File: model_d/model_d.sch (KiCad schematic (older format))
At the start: 50 parts, among them J1 Conn_01x16_Male, J2 Conn_01x08_Male, SW1 SW_Cap, SW10 SW_Cap, SW11 SW_Cap, SW12 SW_Cap, SW13 SW_Cap, SW14 SW_Cap, SW15 SW_Cap, SW16 SW_Cap, SW17 SW_Cap, SW18 SW_Cap, SW19 SW_Cap, SW2 SW_Cap, SW20 SW_Cap, SW21 SW_Cap, SW22 SW_Cap, SW23 SW_Cap, SW24 SW_Cap, SW25 SW_Cap, SW26 SW_Cap, SW27 SW_Cap, SW28 SW_Cap, SW29 SW_Cap, SW3 SW_Cap, SW30 SW_Cap, SW31 SW_Cap, SW32 SW_Cap, SW33 SW_Cap, SW34 SW_Cap, SW35 SW_Cap, SW36 SW_Cap, SW37 SW_Cap, SW38 SW_Cap, SW39 SW_Cap, SW4 SW_Cap, SW40 SW_Cap, SW41 SW_Cap, SW42 SW_Cap, SW43 SW_Cap, SW44 SW_Cap, SW45 SW_Cap, SW46 SW_Cap, SW47 SW_Cap, SW48 SW_Cap, SW5 SW_Cap, SW6 SW_Cap, SW7 SW_Cap, SW8 SW_Cap, SW9 SW_Cap

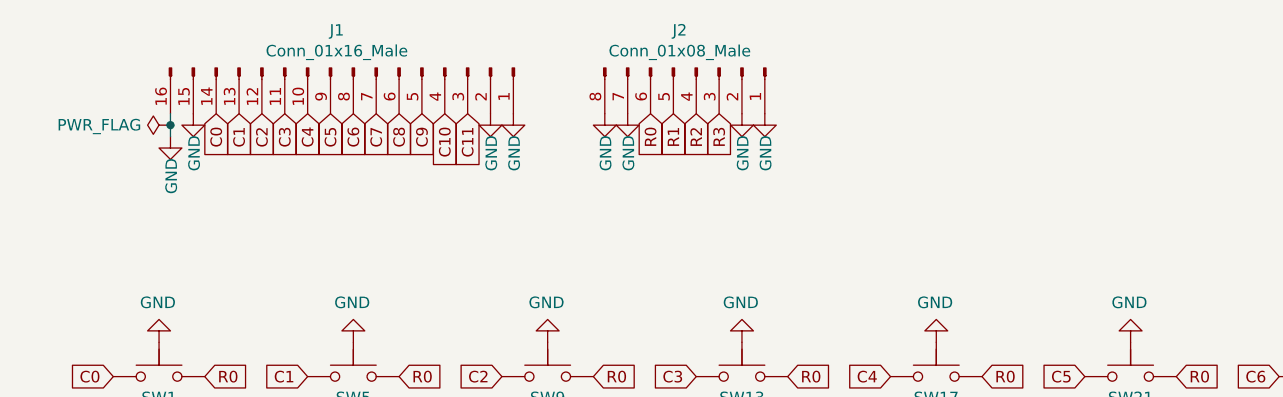
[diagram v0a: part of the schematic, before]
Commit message: complete place & route, add gnd plate
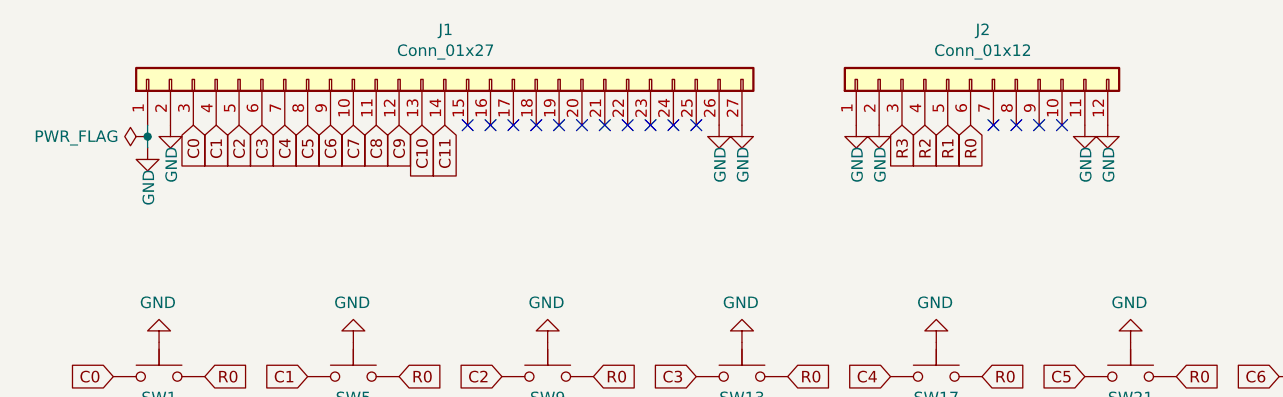
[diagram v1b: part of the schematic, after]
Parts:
- removed J1: Conn_01x16_Male, Connector_PinHeader_2.54mm:PinHeader_1x16_P2.54mm_Vertical, symbol Connector:Conn_01x16_Male
- removed J2: Conn_01x08_Male, Connector_PinHeader_2.54mm:PinHeader_1x08_P2.54mm_Vertical, symbol Connector:Conn_01x08_Male
- added J1: Conn_01x27, Connector_PinHeader_2.54mm:PinHeader_1x27_P2.54mm_Vertical, symbol Connector_Generic:Conn_01x27
- added J2: Conn_01x12, Connector_PinHeader_2.54mm:PinHeader_1x12_P2.54mm_Vertical, symbol Connector_Generic:Conn_01x12
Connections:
- net C0: now also J1.3 (Pin_3)
- net C1: now also J1.4 (Pin_4)
- net C10: now also J1.13 (Pin_13)
- net C11: now also J1.14 (Pin_14)
- net C2: now also J1.5 (Pin_5)
- net C3: now also J1.6 (Pin_6)
- net C4: now also J1.7 (Pin_7)
- net C5: now also J1.8 (Pin_8)
- net C6: now also J1.9 (Pin_9)
- net C7: now also J1.10 (Pin_10)
- net C8: now also J1.11 (Pin_11)
- net C9: now also J1.12 (Pin_12)
- net GND: now also J1.1 (Pin_1), J1.2 (Pin_2), J1.26 (Pin_26), J1.27 (Pin_27), J2.1 (Pin_1), J2.11 (Pin_11), J2.12 (Pin_12), J2.2 (Pin_2)
- net R0: now also J2.6 (Pin_6)
- net R1: now also J2.5 (Pin_5)
- net R2: now also J2.4 (Pin_4)
- net R3: now also J2.3 (Pin_3)
- no-connect marks 0 -> 15
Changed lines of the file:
@@
-$EndComp
-$Comp
-L Connector:Conn_01x16_Male J1
-U 1 1 6176F4F2
-P 2000 1000
-F 0 "J1" V 1835 928 50  0000 C CNN
-F 1 "Conn_01x16_Male" V 1926 928 50  0000 C CNN
-F 2 "Connector_PinHeader_2.54mm:PinHeader_1x16_P2.54mm_Vertical" H 2000 1000 50  0001 C CNN
-F 3 "~" H 2000 1000 50  0001 C CNN
-	1    2000 1000
-	0    1    1    0
 $EndComp
 $Comp
 L power:GND #PWR05
 U 1 1 61773EA7
-P 1200 1300
-F 0 "#PWR05" H 1200 1050 50  0001 C CNN
-F 1 "GND" V 1205 1127 50  0000 C CNN
-F 2 "" H 1200 1300 50  0001 C CNN
-F 3 "" H 1200 1300 50  0001 C CNN
-	1    1200 1300
+P 1100 1350
+F 0 "#PWR05" H 1100 1100 50  0001 C CNN
+F 1 "GND" V 1105 1177 50  0000 C CNN
+F 2 "" H 1100 1350 50  0001 C CNN
+F 3 "" H 1100 1350 50  0001 C CNN
+	1    1100 1350
 	1    0    0    -1
 $EndComp
@@
 L power:GND #PWR06
 U 1 1 61775637
-P 1300 1200
-F 0 "#PWR06" H 1300 950 50  0001 C CNN
-F 1 "GND" V 1305 1027 50  0000 C CNN
-F 2 "" H 1300 1200 50  0001 C CNN
-F 3 "" H 1300 1200 50  0001 C CNN
-	1    1300 1200
+P 1200 1250
+F 0 "#PWR06" H 1200 1000 50  0001 C CNN
+F 1 "GND" V 1205 1077 50  0000 C CNN
+F 2 "" H 1200 1250 50  0001 C CNN
+F 3 "" H 1200 1250 50  0001 C CNN
+	1    1200 1250
 	1    0    0    -1
 $EndComp
@@
 L power:GND #PWR011
 U 1 1 61775AD8
-P 2600 1200
-F 0 "#PWR011" H 2600 950 50  0001 C CNN
-F 1 "GND" V 2605 1027 50  0000 C CNN
-F 2 "" H 2600 1200 50  0001 C CNN
-F 3 "" H 2600 1200 50  0001 C CNN
-	1    2600 1200
+P 3600 1250
+F 0 "#PWR011" H 3600 1000 50  0001 C CNN
+F 1 "GND" V 3605 1077 50  0000 C CNN
+F 2 "" H 3600 1250 50  0001 C CNN
+F 3 "" H 3600 1250 50  0001 C CNN
+	1    3600 1250
 	1    0    0    -1
 $EndComp
@@
 L power:GND #PWR012
 U 1 1 61775FCF
-P 2700 1200
-F 0 "#PWR012" H 2700 950 50  0001 C CNN
-F 1 "GND" V 2705 1027 50  0000 C CNN
-F 2 "" H 2700 1200 50  0001 C CNN
-F 3 "" H 2700 1200 50  0001 C CNN
-	1    2700 1200
+P 3700 1250
+F 0 "#PWR012" H 3700 1000 50  0001 C CNN
+F 1 "GND" V 3705 1077 50  0000 C CNN
+F 2 "" H 3700 1250 50  0001 C CNN
+F 3 "" H 3700 1250 50  0001 C CNN
+	1    3700 1250
 	1    0    0    -1
 $EndComp
-Text GLabel 1400 1200 3    50   Input ~ 0
+Text GLabel 1300 1250 3    50   Input ~ 0
 C0
-Text GLabel 1500 1200 3    50   Input ~ 0
+Text GLabel 1400 1250 3    50   Input ~ 0
 C1
-Text GLabel 1600 1200 3    50   Input ~ 0
+Text GLabel 1500 1250 3    50   Input ~ 0
 C2
-Text GLabel 1800 1200 3    50   Input ~ 0
+Text GLabel 1700 1250 3    50   Input ~ 0
 C4
-Text GLabel 1900 1200 3    50   Input ~ 0
+Text GLabel 1800 1250 3    50   Input ~ 0
 C5
-Text GLabel 2000 1200 3    50   Input ~ 0
+Text GLabel 1900 1250 3    50   Input ~ 0
 C6
-Text GLabel 2100 1200 3    50   Input ~ 0
+Text GLabel 2000 1250 3    50   Input ~ 0
 C7
-Text GLabel 2200 1200 3    50   Input ~ 0
+Text GLabel 2100 1250 3    50   Input ~ 0
 C8
-Text GLabel 2300 1200 3    50   Input ~ 0
+Text GLabel 2200 1250 3    50   Input ~ 0
 C9
-Text GLabel 2400 1200 3    50   Input ~ 0
+Text GLabel 2300 1250 3    50   Input ~ 0
 C10
-Text GLabel 2500 1200 3    50   Input ~ 0
+Text GLabel 2400 1250 3    50   Input ~ 0
 C11
-Text GLabel 1700 1200 3    50   Input ~ 0
+Text GLabel 1600 1250 3    50   Input ~ 0
 C3
-$Comp
-L Connector:Conn_01x08_Male J2
-U 1 1 61788BE2
-P 3500 1000
-F 0 "J2" V 3335 928 50  0000 C CNN
-F 1 "Conn_01x08_Male" V 3426 928 50  0000 C CNN
-F 2 "Connector_PinHeader_2.54mm:PinHeader_1x08_P2.54mm_Vertical" H 3500 1000 50  0001 C CNN
-F 3 "~" H 3500 1000 50  0001 C CNN
-	1    3500 1000
-	0    1    1    0
-$EndComp
 $Comp
 L power:GND #PWR017
 U 1 1 6178BA2D
-P 3100 1200
-F 0 "#PWR017" H 3100 950 50  0001 C CNN
-F 1 "GND" V 3105 1027 50  0000 C CNN
-F 2 "" H 3100 1200 50  0001 C CNN
-F 3 "" H 3100 1200 50  0001 C CNN
-	1    3100 1200
+P 4200 1250
+F 0 "#PWR017" H 4200 1000 50  0001 C CNN
+F 1 "GND" V 4205 1077 50  0000 C CNN
+F 2 "" H 4200 1250 50  0001 C CNN
+F 3 "" H 4200 1250 50  0001 C CNN
+	1    4200 1250
 	1    0    0    -1
 $EndComp
@@
 L power:GND #PWR018
 U 1 1 6178C020
-P 3200 1200
-F 0 "#PWR018" H 3200 950 50  0001 C CNN
-F 1 "GND" V 3205 1027 50  0000 C CNN
-F 2 "" H 3200 1200 50  0001 C CNN
-F 3 "" H 3200 1200 50  0001 C CNN
-	1    3200 1200
+P 4300 1250
+F 0 "#PWR018" H 4300 1000 50  0001 C CNN
+F 1 "GND" V 4305 1077 50  0000 C CNN
+F 2 "" H 4300 1250 50  0001 C CNN
+F 3 "" H 4300 1250 50  0001 C CNN
+	1    4300 1250
 	1    0    0    -1
 $EndComp
@@
 L power:GND #PWR019
 U 1 1 6178C499
-P 3700 1200
-F 0 "#PWR019" H 3700 950 50  0001 C CNN
-F 1 "GND" V 3705 1027 50  0000 C CNN
-F 2 "" H 3700 1200 50  0001 C CNN
-F 3 "" H 3700 1200 50  0001 C CNN
-	1    3700 1200
+P 5200 1250
+F 0 "#PWR019" H 5200 1000 50  0001 C CNN
+F 1 "GND" V 5205 1077 50  0000 C CNN
+F 2 "" H 5200 1250 50  0001 C CNN
+F 3 "" H 5200 1250 50  0001 C CNN
+	1    5200 1250
 	1    0    0    -1
 $EndComp
@@
 L power:GND #PWR024
 U 1 1 6178CA31
-P 3800 1200
-F 0 "#PWR024" H 3800 950 50  0001 C CNN
-F 1 "GND" V 3805 1027 50  0000 C CNN
-F 2 "" H 3800 1200 50  0001 C CNN
-F 3 "" H 3800 1200 50  0001 C CNN
-	1    3800 1200
+P 5300 1250
+F 0 "#PWR024" H 5300 1000 50  0001 C CNN
+F 1 "GND" V 5305 1077 50  0000 C CNN
+F 2 "" H 5300 1250 50  0001 C CNN
+F 3 "" H 5300 1250 50  0001 C CNN
+	1    5300 1250
 	1    0    0    -1
 $EndComp
-Text GLabel 3300 1200 3    50   Input ~ 0
+Text GLabel 4700 1250 3    50   Input ~ 0
 R0
-Text GLabel 3400 1200 3    50   Input ~ 0
+Text GLabel 4600 1250 3    50   Input ~ 0
 R1
-Text GLabel 3500 1200 3    50   Input ~ 0
+Text GLabel 4500 1250 3    50   Input ~ 0
 R2
-Text GLabel 3600 1200 3    50   Input ~ 0
+Text GLabel 4400 1250 3    50   Input ~ 0
 R3
 $Comp
 L power:PWR_FLAG #FLG0101
 U 1 1 617950E2
-P 1200 1250
-F 0 "#FLG0101" H 1200 1325 50  0001 C CNN
-F 1 "PWR_FLAG" V 1200 1377 50  0000 L CNN
-F 2 "" H 1200 1250 50  0001 C CNN
-F 3 "~" H 1200 1250 50  0001 C CNN
-	1    1200 1250
+P 1100 1300
+F 0 "#FLG0101" H 1100 1375 50  0001 C CNN
+F 1 "PWR_FLAG" V 1100 1427 50  0000 L CNN
+F 2 "" H 1100 1300 50  0001 C CNN
+F 3 "~" H 1100 1300 50  0001 C CNN
+	1    1100 1300
 	0    -1   -1   0
 $EndComp
 Wire Wire Line
-	1200 1300 1200 1250
+	1100 1350 1100 1300
 Wire Wire Line
-	1200 1250 1200 1200
-Connection ~ 1200 1250
+	1100 1300 1100 1250
+$Comp
+L Connector_Generic:Conn_01x27 J1
+U 1 1 616B3F4A
+P 2400 1050
+F 0 "J1" V 2617 1046 50  0000 C CNN
+F 1 "Conn_01x27" V 2526 1046 50  0000 C CNN
+F 2 "Connector_PinHeader_2.54mm:PinHeader_1x27_P2.54mm_Vertical" H 2400 1050 50  0001 C CNN
+F 3 "~" H 2400 1050 50  0001 C CNN
+	1    2400 1050
+	0    -1   -1   0
+$EndComp
+Connection ~ 1100 1300
+NoConn ~ 2500 1250
+NoConn ~ 2600 1250
+NoConn ~ 2700 1250
+NoConn ~ 2800 1250
+NoConn ~ 2900 1250
+NoConn ~ 3000 1250
+NoConn ~ 3100 1250
+NoConn ~ 3200 1250
+NoConn ~ 3300 1250
+NoConn ~ 3400 1250
+NoConn ~ 3500 1250
+$Comp
+L Connector_Generic:Conn_01x12 J2
+U 1 1 61709475
+P 4700 1050
+F 0 "J2" V 4917 996 50  0000 C CNN
+F 1 "Conn_01x12" V 4826 996 50  0000 C CNN
+F 2 "Connector_PinHeader_2.54mm:PinHeader_1x12_P2.54mm_Vertical" H 4700 1050 50  0001 C CNN
+F 3 "~" H 4700 1050 50  0001 C CNN
+	1    4700 1050
+	0    -1   -1   0
+$EndComp
+NoConn ~ 4800 1250
+NoConn ~ 4900 1250
+NoConn ~ 5000 1250
+NoConn ~ 5100 1250
 $EndSCHEMATC

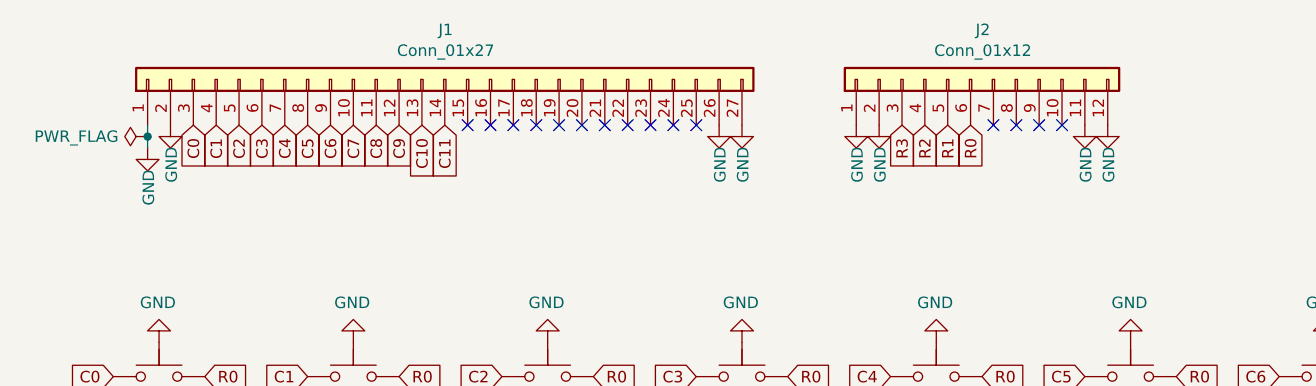
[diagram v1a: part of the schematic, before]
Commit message: add m3 mounting holes, increase size to 113x244
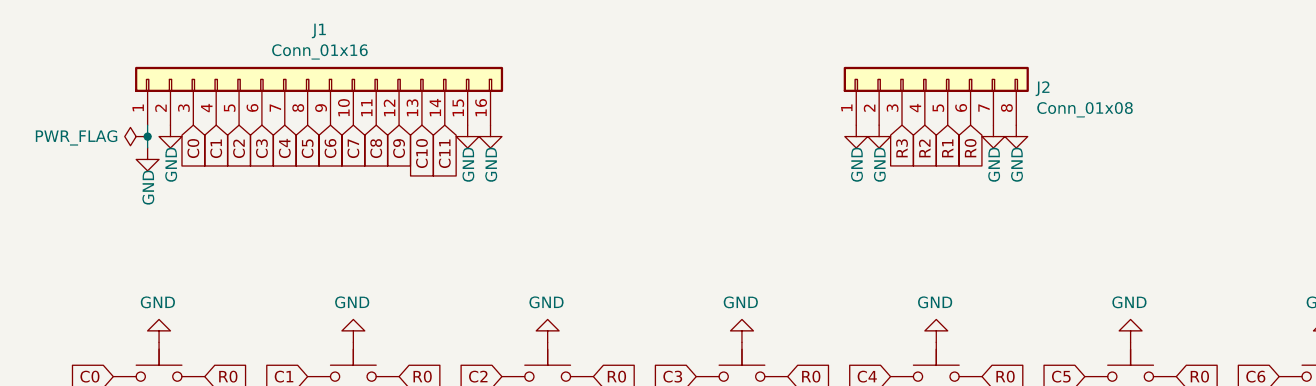
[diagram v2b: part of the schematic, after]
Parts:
- removed J1: Conn_01x27, Connector_PinHeader_2.54mm:PinHeader_1x27_P2.54mm_Vertical, symbol Connector_Generic:Conn_01x27
- removed J2: Conn_01x12, Connector_PinHeader_2.54mm:PinHeader_1x12_P2.54mm_Vertical, symbol Connector_Generic:Conn_01x12
- added J1: Conn_01x16, Connector_PinHeader_2.54mm:PinHeader_1x16_P2.54mm_Vertical, symbol Connector_Generic:Conn_01x16
- added J2: Conn_01x08, Connector_PinHeader_2.54mm:PinHeader_1x08_P2.54mm_Vertical, symbol Connector_Generic:Conn_01x08
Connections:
- net C0: now also J1.3 (Pin_3)
- net C1: now also J1.4 (Pin_4)
- net C10: now also J1.13 (Pin_13)
- net C11: now also J1.14 (Pin_14)
- net C2: now also J1.5 (Pin_5)
- net C3: now also J1.6 (Pin_6)
- net C4: now also J1.7 (Pin_7)
- net C5: now also J1.8 (Pin_8)
- net C6: now also J1.9 (Pin_9)
- net C7: now also J1.10 (Pin_10)
- net C8: now also J1.11 (Pin_11)
- net C9: now also J1.12 (Pin_12)
- net GND: now also J1.1 (Pin_1), J1.15 (Pin_15), J1.16 (Pin_16), J1.2 (Pin_2), J2.1 (Pin_1), J2.2 (Pin_2), J2.7 (Pin_7), J2.8 (Pin_8)
- net R0: now also J2.6 (Pin_6)
- net R1: now also J2.5 (Pin_5)
- net R2: now also J2.4 (Pin_4)
- net R3: now also J2.3 (Pin_3)
- no-connect marks 15 -> 0
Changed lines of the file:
@@
 L power:GND #PWR011
 U 1 1 61775AD8
-P 3600 1250
-F 0 "#PWR011" H 3600 1000 50  0001 C CNN
-F 1 "GND" V 3605 1077 50  0000 C CNN
-F 2 "" H 3600 1250 50  0001 C CNN
-F 3 "" H 3600 1250 50  0001 C CNN
-	1    3600 1250
+P 2500 1250
+F 0 "#PWR011" H 2500 1000 50  0001 C CNN
+F 1 "GND" V 2505 1077 50  0000 C CNN
+F 2 "" H 2500 1250 50  0001 C CNN
+F 3 "" H 2500 1250 50  0001 C CNN
+	1    2500 1250
 	1    0    0    -1
 $EndComp
@@
 L power:GND #PWR012
 U 1 1 61775FCF
-P 3700 1250
-F 0 "#PWR012" H 3700 1000 50  0001 C CNN
-F 1 "GND" V 3705 1077 50  0000 C CNN
-F 2 "" H 3700 1250 50  0001 C CNN
-F 3 "" H 3700 1250 50  0001 C CNN
-	1    3700 1250
+P 2600 1250
+F 0 "#PWR012" H 2600 1000 50  0001 C CNN
+F 1 "GND" V 2605 1077 50  0000 C CNN
+F 2 "" H 2600 1250 50  0001 C CNN
+F 3 "" H 2600 1250 50  0001 C CNN
+	1    2600 1250
 	1    0    0    -1
 $EndComp
@@
 L power:GND #PWR019
 U 1 1 6178C499
-P 5200 1250
-F 0 "#PWR019" H 5200 1000 50  0001 C CNN
-F 1 "GND" V 5205 1077 50  0000 C CNN
-F 2 "" H 5200 1250 50  0001 C CNN
-F 3 "" H 5200 1250 50  0001 C CNN
-	1    5200 1250
+P 4800 1250
+F 0 "#PWR019" H 4800 1000 50  0001 C CNN
+F 1 "GND" V 4805 1077 50  0000 C CNN
+F 2 "" H 4800 1250 50  0001 C CNN
+F 3 "" H 4800 1250 50  0001 C CNN
+	1    4800 1250
 	1    0    0    -1
 $EndComp
@@
 L power:GND #PWR024
 U 1 1 6178CA31
-P 5300 1250
-F 0 "#PWR024" H 5300 1000 50  0001 C CNN
-F 1 "GND" V 5305 1077 50  0000 C CNN
-F 2 "" H 5300 1250 50  0001 C CNN
-F 3 "" H 5300 1250 50  0001 C CNN
-	1    5300 1250
+P 4900 1250
+F 0 "#PWR024" H 4900 1000 50  0001 C CNN
+F 1 "GND" V 4905 1077 50  0000 C CNN
+F 2 "" H 4900 1250 50  0001 C CNN
+F 3 "" H 4900 1250 50  0001 C CNN
+	1    4900 1250
 	1    0    0    -1
 $EndComp
@@
 Wire Wire Line
 	1100 1300 1100 1250
+Connection ~ 1100 1300
 $Comp
-L Connector_Generic:Conn_01x27 J1
-U 1 1 616B3F4A
-P 2400 1050
-F 0 "J1" V 2617 1046 50  0000 C CNN
-F 1 "Conn_01x27" V 2526 1046 50  0000 C CNN
-F 2 "Connector_PinHeader_2.54mm:PinHeader_1x27_P2.54mm_Vertical" H 2400 1050 50  0001 C CNN
-F 3 "~" H 2400 1050 50  0001 C CNN
-	1    2400 1050
+L Connector_Generic:Conn_01x16 J1
+U 1 1 61CCE509
+P 1800 1050
+F 0 "J1" V 2017 996 50  0000 C CNN
+F 1 "Conn_01x16" V 1926 996 50  0000 C CNN
+F 2 "Connector_PinHeader_2.54mm:PinHeader_1x16_P2.54mm_Vertical" H 1800 1050 50  0001 C CNN
+F 3 "~" H 1800 1050 50  0001 C CNN
+	1    1800 1050
 	0    -1   -1   0
 $EndComp
-Connection ~ 1100 1300
-NoConn ~ 2500 1250
-NoConn ~ 2600 1250
-NoConn ~ 2700 1250
-NoConn ~ 2800 1250
-NoConn ~ 2900 1250
-NoConn ~ 3000 1250
-NoConn ~ 3100 1250
-NoConn ~ 3200 1250
-NoConn ~ 3300 1250
-NoConn ~ 3400 1250
-NoConn ~ 3500 1250
 $Comp
-L Connector_Generic:Conn_01x12 J2
-U 1 1 61709475
-P 4700 1050
-F 0 "J2" V 4917 996 50  0000 C CNN
-F 1 "Conn_01x12" V 4826 996 50  0000 C CNN
-F 2 "Connector_PinHeader_2.54mm:PinHeader_1x12_P2.54mm_Vertical" H 4700 1050 50  0001 C CNN
-F 3 "~" H 4700 1050 50  0001 C CNN
-	1    4700 1050
+L Connector_Generic:Conn_01x08 J2
+U 1 1 61CE709E
+P 4500 1050
+F 0 "J2" V 4464 562 50  0000 R CNN
+F 1 "Conn_01x08" V 4373 562 50  0000 R CNN
+F 2 "Connector_PinHeader_2.54mm:PinHeader_1x08_P2.54mm_Vertical" H 4500 1050 50  0001 C CNN
+F 3 "~" H 4500 1050 50  0001 C CNN
+	1    4500 1050
 	0    -1   -1   0
 $EndComp
-NoConn ~ 4800 1250
-NoConn ~ 4900 1250
-NoConn ~ 5000 1250
-NoConn ~ 5100 1250
 $EndSCHEMATC
